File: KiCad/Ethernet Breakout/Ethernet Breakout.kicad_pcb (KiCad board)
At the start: 2 copper layers, 25.7 x 19 mm, 4 parts, among them J1 Conn_01x04

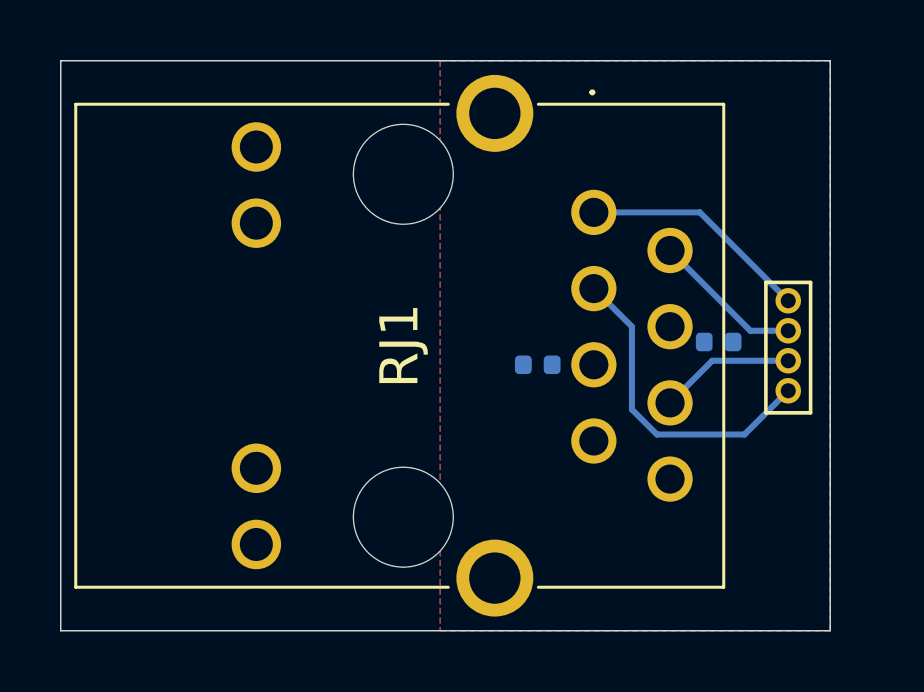
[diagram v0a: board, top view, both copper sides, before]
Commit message: Finalized Ethernet Breakout for production
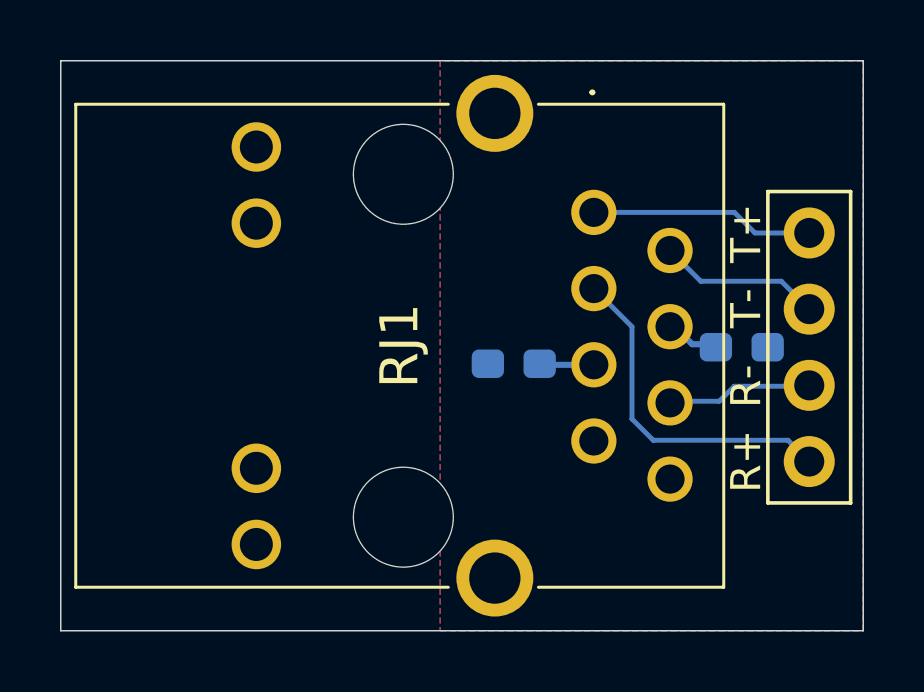
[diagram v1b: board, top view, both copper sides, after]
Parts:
- C2, C3: footprint Capacitor_SMD:C_0402_1005Metric -> Capacitor_SMD:C_0603_1608Metric_Pad1.08x0.95mm_HandSolder
- J1: footprint Connector_PinHeader_1.00mm:PinHeader_1x04_P1.00mm_Vertical -> Connector_PinHeader_2.54mm:PinHeader_1x04_P2.54mm_Vertical
- moved J1 2.46 mm to (138.3, 96.6)
- moved C2 0.80 mm to (128.4, 93.3)
- moved C3 0.79 mm to (136.1, 92.8)
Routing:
- net Net-(C2-Pad2): track 0.00 -> 2.28 mm
- net Net-(C3-Pad2): track 0.00 -> 1.81 mm
- net /RX+: track 10.7 -> 11.4 mm
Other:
- board size 25.7 x 19 mm -> 26.8 x 19 mm
- board text added: "R+"
- board text added: "R-"
- board text added: "T+"
- board text added: "T-"
